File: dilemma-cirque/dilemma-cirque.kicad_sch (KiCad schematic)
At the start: 9 parts, among them J1 CirqueDB

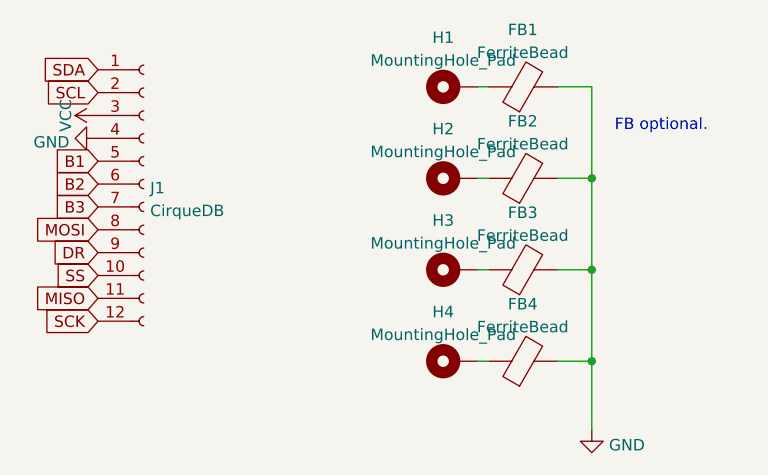
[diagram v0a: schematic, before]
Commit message: Footprint library created, CirqueDB more compact
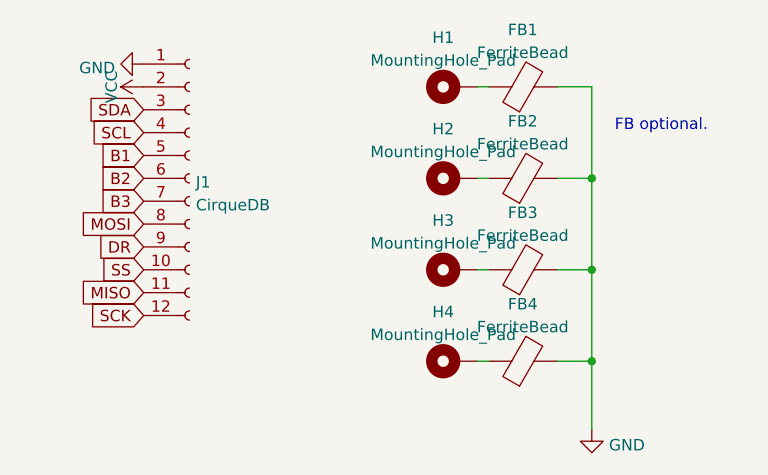
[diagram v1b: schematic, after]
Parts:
- FB1, FB2, FB3, FB4: footprint Inductor_SMD:L_0805_2012Metric_Pad1.15x1.40mm_HandSolder -> BKCirqueDB:L_0805_2012Metric_Pad1.15x1.40mm_HandSolder
- H1, H2, H3, H4: footprint MountingHole:MountingHole_3.2mm_M3_DIN965_Pad -> BKCirqueDB:MountingHole_2.2mm_M2_Pad
- J1: footprint prettylib:CirqueDB-BK -> BKCirqueDB:CirqueDB_compact-BK
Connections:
- net GND: now also J1.1 (Pin_1); no longer J1.4 (Pin_4)
- net SCL: now also J1.4 (Pin_4); no longer J1.2 (Pin_2)
- net SDA: now also J1.3 (Pin_3); no longer J1.1 (Pin_1)
- net VCC: now also J1.2 (Pin_2); no longer J1.3 (Pin_3)
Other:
- moved on the sheet: J1

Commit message: M2 to M3
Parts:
- H1, H2, H3, H4: footprint BKCirqueDB:MountingHole_2.2mm_M2_Pad -> MountingHole:MountingHole_3mm_Pad
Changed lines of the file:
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@@
     (property "Reference" "H3" (id 0) (at 66.294 40.2422 90))
     (property "Value" "MountingHole_Pad" (id 1) (at 66.294 42.7791 90))
-    (property "Footprint" "BKCirqueDB:MountingHole_2.2mm_M2_Pad" (id 2) (at 67.564 45.72 0)
+    (property "Footprint" "MountingHole:MountingHole_3mm_Pad" (id 2) (at 67.564 45.72 0)
       (effects (font (size 1.27 1.27)) hide)
     )
@@
     (property "Reference" "H1" (id 0) (at 66.294 19.9222 90))
     (property "Value" "MountingHole_Pad" (id 1) (at 66.294 22.4591 90))
-    (property "Footprint" "BKCirqueDB:MountingHole_2.2mm_M2_Pad" (id 2) (at 67.564 25.4 0)
+    (property "Footprint" "MountingHole:MountingHole_3mm_Pad" (id 2) (at 67.564 25.4 0)
       (effects (font (size 1.27 1.27)) hide)
     )
@@
     (property "Reference" "H4" (id 0) (at 66.294 50.4022 90))
     (property "Value" "MountingHole_Pad" (id 1) (at 66.294 52.9391 90))
-    (property "Footprint" "BKCirqueDB:MountingHole_2.2mm_M2_Pad" (id 2) (at 67.564 55.88 0)
+    (property "Footprint" "MountingHole:MountingHole_3mm_Pad" (id 2) (at 67.564 55.88 0)
       (effects (font (size 1.27 1.27)) hide)
     )
@@
     (property "Reference" "H2" (id 0) (at 66.294 30.0822 90))
     (property "Value" "MountingHole_Pad" (id 1) (at 66.294 32.6191 90))
-    (property "Footprint" "BKCirqueDB:MountingHole_2.2mm_M2_Pad" (id 2) (at 67.564 35.56 0)
+    (property "Footprint" "MountingHole:MountingHole_3mm_Pad" (id 2) (at 67.564 35.56 0)
       (effects (font (size 1.27 1.27)) hide)
     )
@@
     )
     (path "/17c88554-b84a-4558-a973-bb4ec16ea7b6"
-      (reference "H1") (unit 1) (value "MountingHole_Pad") (footprint "BKCirqueDB:MountingHole_2.2mm_M2_Pad")
+      (reference "H1") (unit 1) (value "MountingHole_Pad") (footprint "MountingHole:MountingHole_3mm_Pad")
     )
     (path "/f515a122-b419-4a67-b625-1d6b443c7959"
-      (reference "H2") (unit 1) (value "MountingHole_Pad") (footprint "BKCirqueDB:MountingHole_2.2mm_M2_Pad")
+      (reference "H2") (unit 1) (value "MountingHole_Pad") (footprint "MountingHole:MountingHole_3mm_Pad")
     )
     (path "/0cee515e-bff0-441c-808f-5c7f575531ab"
-      (reference "H3") (unit 1) (value "MountingHole_Pad") (footprint "BKCirqueDB:MountingHole_2.2mm_M2_Pad")
+      (reference "H3") (unit 1) (value "MountingHole_Pad") (footprint "MountingHole:MountingHole_3mm_Pad")
     )
     (path "/632c8793-0a5e-4b9e-8fad-8505a760b4eb"
-      (reference "H4") (unit 1) (value "MountingHole_Pad") (footprint "BKCirqueDB:MountingHole_2.2mm_M2_Pad")
+      (reference "H4") (unit 1) (value "MountingHole_Pad") (footprint "MountingHole:MountingHole_3mm_Pad")
     )
     (path "/0c15bea0-7570-445f-946c-68b28e4351f3"
